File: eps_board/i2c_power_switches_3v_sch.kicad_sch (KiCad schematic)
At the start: 10 parts, among them U30 MCP23017T-E/SS

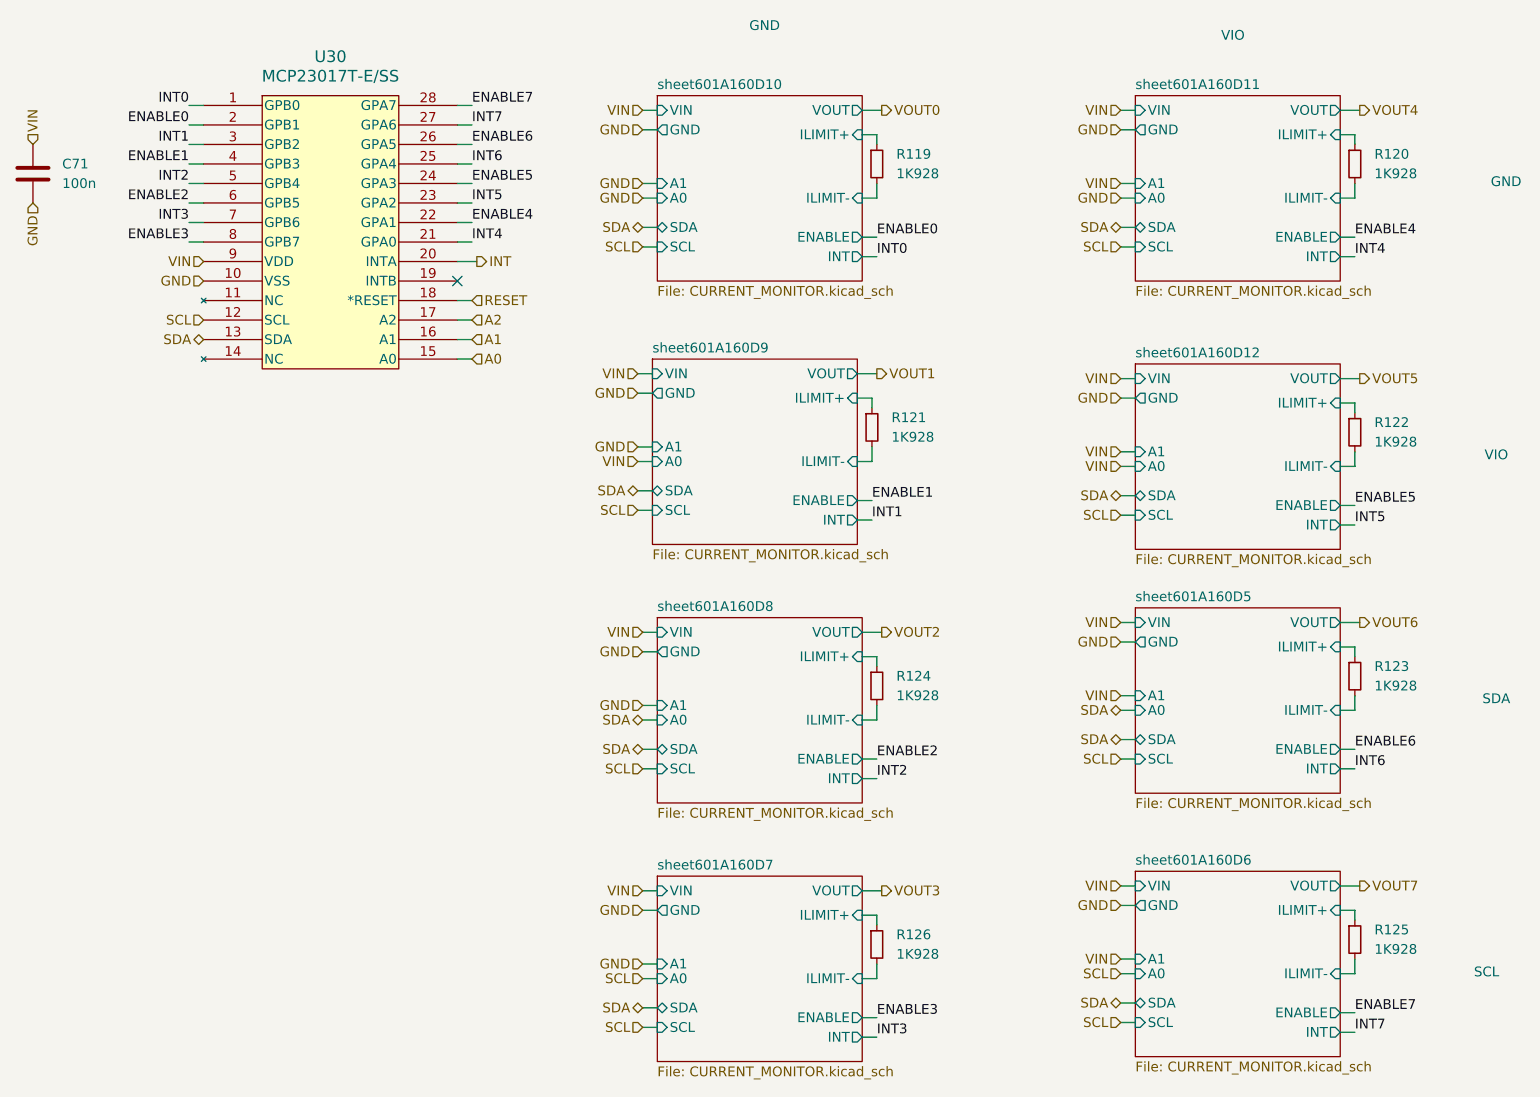
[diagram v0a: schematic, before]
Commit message: simply eps and automate startup conditions
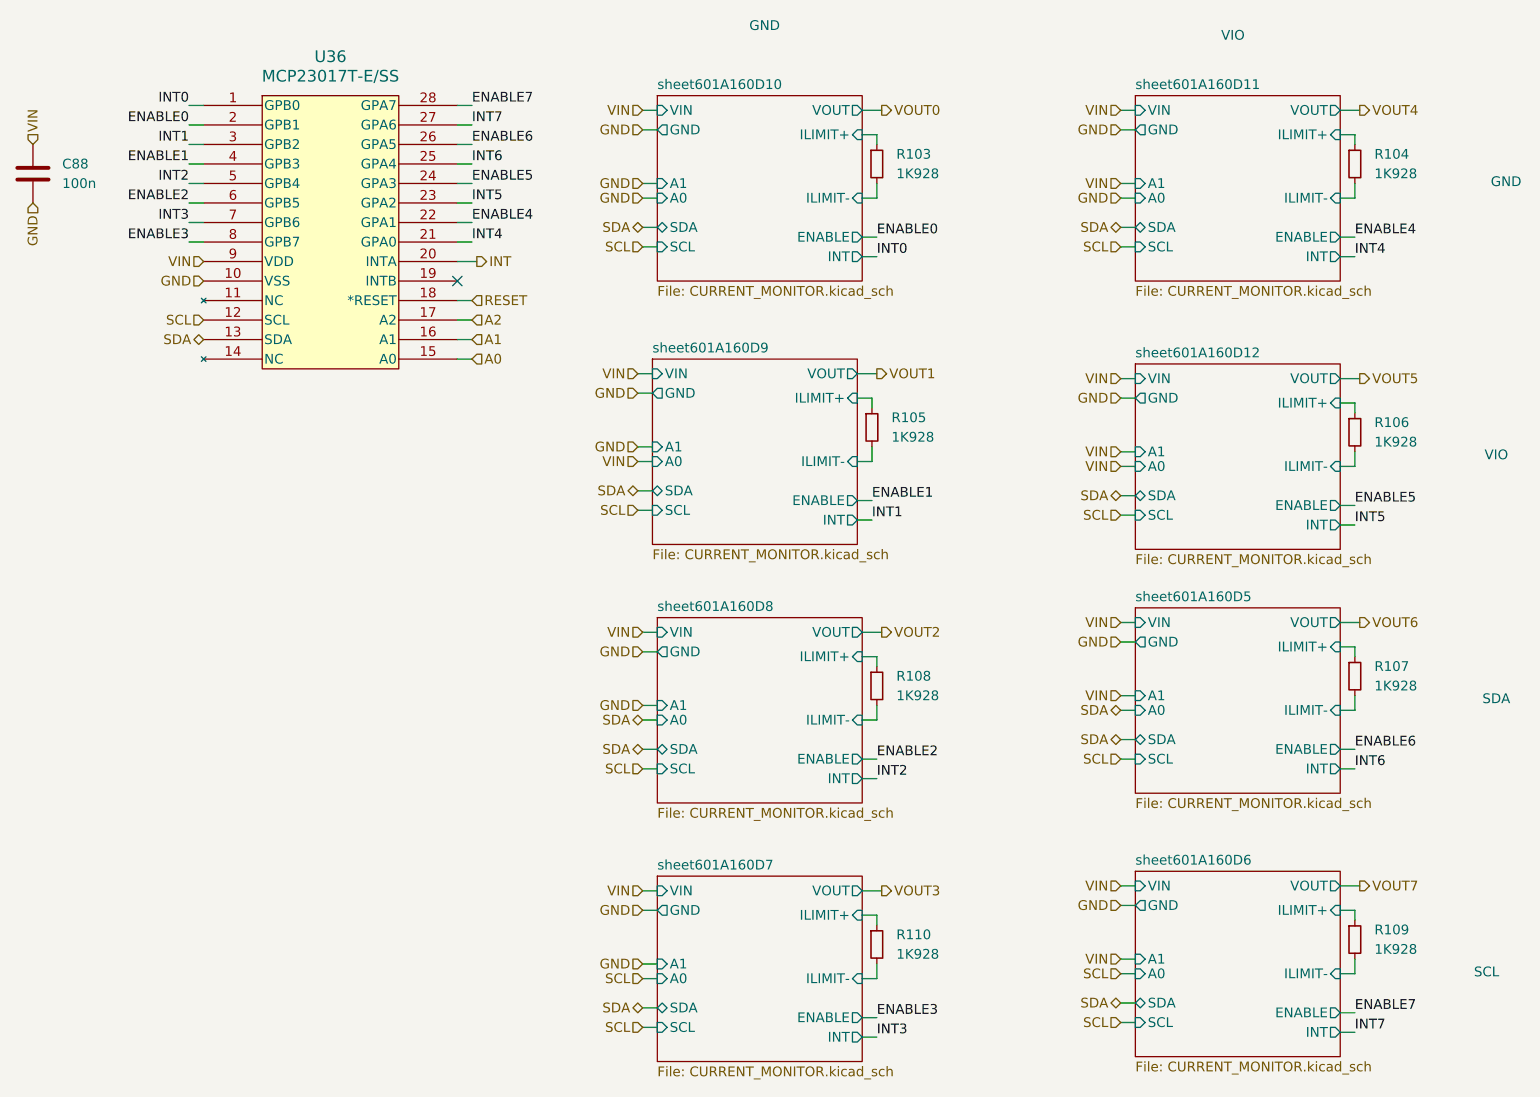
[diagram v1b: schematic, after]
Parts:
- renumbered C71 to C88, R119 to R103, R120 to R104, R121 to R105, R122 to R106, R123 to R107, R124 to R108, R125 to R109, R126 to R110, U30 to U36
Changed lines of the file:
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@@
 		(dnp no)
 		(fields_autoplaced yes)
-		(property "Reference" "U30"
+		(property "Reference" "U36"
 			(at 60.325 27.94 0)
 			(effects
@@
 			(project ""
 				(path "/05170af6-30ef-4c3a-b972-f098085da1bc/365e30aa-57e3-49e2-b136-6964bfe03313"
-					(reference "U30")
-					(unit 1)
-				)
-				(path "/05170af6-30ef-4c3a-b972-f098085da1bc/87d4360e-0b9f-4926-a66e-357599f9c0d1"
-					(reference "U48")
+					(reference "U36")
+					(unit 1)
+				)
+				(path "/05170af6-30ef-4c3a-b972-f098085da1bc/87d4360e-0b9f-4926-a66e-357599f9c0d1"
+					(reference "U56")
 					(unit 1)
 				)
@@
 		(dnp no)
 		(fields_autoplaced yes)
-		(property "Reference" "R123"
+		(property "Reference" "R107"
 			(at 196.215 107.3149 0)
 			(effects
@@
 			(project "EPS"
 				(path "/05170af6-30ef-4c3a-b972-f098085da1bc/365e30aa-57e3-49e2-b136-6964bfe03313"
-					(reference "R123")
-					(unit 1)
-				)
-				(path "/05170af6-30ef-4c3a-b972-f098085da1bc/87d4360e-0b9f-4926-a66e-357599f9c0d1"
-					(reference "R149")
+					(reference "R107")
+					(unit 1)
+				)
+				(path "/05170af6-30ef-4c3a-b972-f098085da1bc/87d4360e-0b9f-4926-a66e-357599f9c0d1"
+					(reference "R147")
 					(unit 1)
 				)
@@
 		(dnp no)
 		(fields_autoplaced yes)
-		(property "Reference" "R122"
+		(property "Reference" "R106"
 			(at 196.215 75.5649 0)
 			(effects
@@
 			(project "EPS"
 				(path "/05170af6-30ef-4c3a-b972-f098085da1bc/365e30aa-57e3-49e2-b136-6964bfe03313"
-					(reference "R122")
-					(unit 1)
-				)
-				(path "/05170af6-30ef-4c3a-b972-f098085da1bc/87d4360e-0b9f-4926-a66e-357599f9c0d1"
-					(reference "R148")
+					(reference "R106")
+					(unit 1)
+				)
+				(path "/05170af6-30ef-4c3a-b972-f098085da1bc/87d4360e-0b9f-4926-a66e-357599f9c0d1"
+					(reference "R146")
 					(unit 1)
 				)
@@
 		(dnp no)
 		(fields_autoplaced yes)
-		(property "Reference" "R124"
+		(property "Reference" "R108"
 			(at 133.985 108.5849 0)
 			(effects
@@
 			(project "EPS"
 				(path "/05170af6-30ef-4c3a-b972-f098085da1bc/365e30aa-57e3-49e2-b136-6964bfe03313"
-					(reference "R124")
-					(unit 1)
-				)
-				(path "/05170af6-30ef-4c3a-b972-f098085da1bc/87d4360e-0b9f-4926-a66e-357599f9c0d1"
-					(reference "R150")
+					(reference "R108")
+					(unit 1)
+				)
+				(path "/05170af6-30ef-4c3a-b972-f098085da1bc/87d4360e-0b9f-4926-a66e-357599f9c0d1"
+					(reference "R148")
 					(unit 1)
 				)
@@
 		(dnp no)
 		(fields_autoplaced yes)
-		(property "Reference" "R125"
+		(property "Reference" "R109"
 			(at 196.215 141.6049 0)
 			(effects
@@
 			(project "EPS"
 				(path "/05170af6-30ef-4c3a-b972-f098085da1bc/365e30aa-57e3-49e2-b136-6964bfe03313"
-					(reference "R125")
-					(unit 1)
-				)
-				(path "/05170af6-30ef-4c3a-b972-f098085da1bc/87d4360e-0b9f-4926-a66e-357599f9c0d1"
-					(reference "R151")
+					(reference "R109")
+					(unit 1)
+				)
+				(path "/05170af6-30ef-4c3a-b972-f098085da1bc/87d4360e-0b9f-4926-a66e-357599f9c0d1"
+					(reference "R149")
 					(unit 1)
 				)
@@
 		(dnp no)
 		(fields_autoplaced yes)
-		(property "Reference" "R119"
+		(property "Reference" "R103"
 			(at 133.985 40.6399 0)
 			(effects
@@
 			(project "EPS"
 				(path "/05170af6-30ef-4c3a-b972-f098085da1bc/365e30aa-57e3-49e2-b136-6964bfe03313"
-					(reference "R119")
-					(unit 1)
-				)
-				(path "/05170af6-30ef-4c3a-b972-f098085da1bc/87d4360e-0b9f-4926-a66e-357599f9c0d1"
-					(reference "R145")
+					(reference "R103")
+					(unit 1)
+				)
+				(path "/05170af6-30ef-4c3a-b972-f098085da1bc/87d4360e-0b9f-4926-a66e-357599f9c0d1"
+					(reference "R143")
 					(unit 1)
 				)
@@
 		(dnp no)
 		(fields_autoplaced yes)
-		(property "Reference" "R126"
+		(property "Reference" "R110"
 			(at 133.985 142.2399 0)
 			(effects
@@
 			(project "EPS"
 				(path "/05170af6-30ef-4c3a-b972-f098085da1bc/365e30aa-57e3-49e2-b136-6964bfe03313"
-					(reference "R126")
-					(unit 1)
-				)
-				(path "/05170af6-30ef-4c3a-b972-f098085da1bc/87d4360e-0b9f-4926-a66e-357599f9c0d1"
-					(reference "R152")
+					(reference "R110")
+					(unit 1)
+				)
+				(path "/05170af6-30ef-4c3a-b972-f098085da1bc/87d4360e-0b9f-4926-a66e-357599f9c0d1"
+					(reference "R150")
 					(unit 1)
 				)
@@
 		(dnp no)
 		(fields_autoplaced yes)
-		(property "Reference" "R121"
+		(property "Reference" "R105"
 			(at 133.35 74.9299 0)
 			(effects
@@
 			(project "EPS"
 				(path "/05170af6-30ef-4c3a-b972-f098085da1bc/365e30aa-57e3-49e2-b136-6964bfe03313"
-					(reference "R121")
-					(unit 1)
-				)
-				(path "/05170af6-30ef-4c3a-b972-f098085da1bc/87d4360e-0b9f-4926-a66e-357599f9c0d1"
-					(reference "R147")
+					(reference "R105")
+					(unit 1)
+				)
+				(path "/05170af6-30ef-4c3a-b972-f098085da1bc/87d4360e-0b9f-4926-a66e-357599f9c0d1"
+					(reference "R145")
 					(unit 1)
 				)
@@
 		(dnp no)
 		(fields_autoplaced yes)
-		(property "Reference" "C71"
+		(property "Reference" "C88"
 			(at 25.4 41.9099 0)
 			(effects
@@
 			(project "EPS"
 				(path "/05170af6-30ef-4c3a-b972-f098085da1bc/365e30aa-57e3-49e2-b136-6964bfe03313"
-					(reference "C71")
-					(unit 1)
-				)
-				(path "/05170af6-30ef-4c3a-b972-f098085da1bc/87d4360e-0b9f-4926-a66e-357599f9c0d1"
-					(reference "C97")
+					(reference "C88")
+					(unit 1)
+				)
+				(path "/05170af6-30ef-4c3a-b972-f098085da1bc/87d4360e-0b9f-4926-a66e-357599f9c0d1"
+					(reference "C116")
 					(unit 1)
 				)
@@
 		(dnp no)
 		(fields_autoplaced yes)
-		(property "Reference" "R120"
+		(property "Reference" "R104"
 			(at 196.215 40.6399 0)
 			(effects
@@
 			(project "EPS"
 				(path "/05170af6-30ef-4c3a-b972-f098085da1bc/365e30aa-57e3-49e2-b136-6964bfe03313"
-					(reference "R120")
-					(unit 1)
-				)
-				(path "/05170af6-30ef-4c3a-b972-f098085da1bc/87d4360e-0b9f-4926-a66e-357599f9c0d1"
-					(reference "R146")
-					(unit 1)
-				)
+					(reference "R104")
+					(unit 1)
+				)
+				(path "/05170af6-30ef-4c3a-b972-f098085da1bc/87d4360e-0b9f-4926-a66e-357599f9c0d1"
+					(reference "R144")
+					(unit 1)
+				)

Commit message: pcb and silk screen cleanup, interim
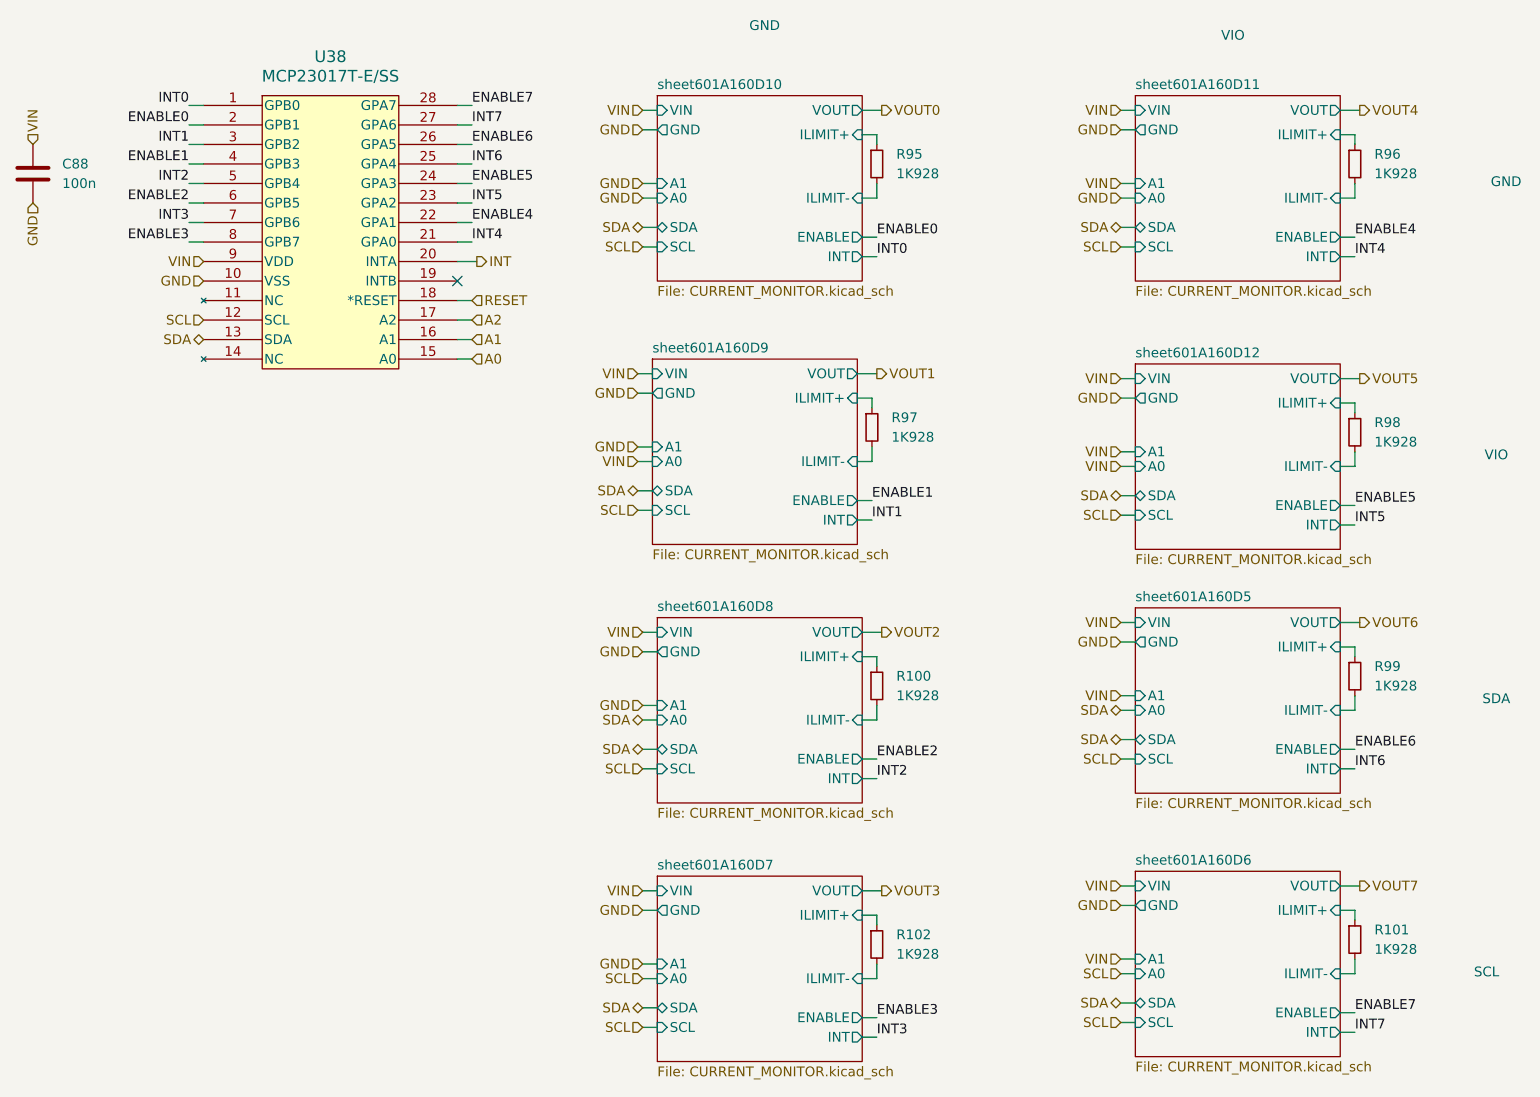
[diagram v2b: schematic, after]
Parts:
- renumbered R108 to R100, R109 to R101, R110 to R102, R103 to R95, R104 to R96, R105 to R97, R106 to R98, R107 to R99, U36 to U38
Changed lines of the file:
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@@
 		(dnp no)
 		(fields_autoplaced yes)
-		(property "Reference" "U36"
+		(property "Reference" "U38"
 			(at 60.325 27.94 0)
 			(effects
@@
 			(project ""
 				(path "/05170af6-30ef-4c3a-b972-f098085da1bc/365e30aa-57e3-49e2-b136-6964bfe03313"
-					(reference "U36")
-					(unit 1)
-				)
-				(path "/05170af6-30ef-4c3a-b972-f098085da1bc/87d4360e-0b9f-4926-a66e-357599f9c0d1"
-					(reference "U56")
+					(reference "U38")
+					(unit 1)
+				)
+				(path "/05170af6-30ef-4c3a-b972-f098085da1bc/87d4360e-0b9f-4926-a66e-357599f9c0d1"
+					(reference "U58")
 					(unit 1)
 				)
@@
 		(dnp no)
 		(fields_autoplaced yes)
-		(property "Reference" "R107"
+		(property "Reference" "R99"
 			(at 196.215 107.3149 0)
 			(effects
@@
 			(project "EPS"
 				(path "/05170af6-30ef-4c3a-b972-f098085da1bc/365e30aa-57e3-49e2-b136-6964bfe03313"
-					(reference "R107")
-					(unit 1)
-				)
-				(path "/05170af6-30ef-4c3a-b972-f098085da1bc/87d4360e-0b9f-4926-a66e-357599f9c0d1"
-					(reference "R147")
+					(reference "R99")
+					(unit 1)
+				)
+				(path "/05170af6-30ef-4c3a-b972-f098085da1bc/87d4360e-0b9f-4926-a66e-357599f9c0d1"
+					(reference "R139")
 					(unit 1)
 				)
@@
 		(dnp no)
 		(fields_autoplaced yes)
-		(property "Reference" "R106"
+		(property "Reference" "R98"
 			(at 196.215 75.5649 0)
 			(effects
@@
 			(project "EPS"
 				(path "/05170af6-30ef-4c3a-b972-f098085da1bc/365e30aa-57e3-49e2-b136-6964bfe03313"
-					(reference "R106")
-					(unit 1)
-				)
-				(path "/05170af6-30ef-4c3a-b972-f098085da1bc/87d4360e-0b9f-4926-a66e-357599f9c0d1"
-					(reference "R146")
+					(reference "R98")
+					(unit 1)
+				)
+				(path "/05170af6-30ef-4c3a-b972-f098085da1bc/87d4360e-0b9f-4926-a66e-357599f9c0d1"
+					(reference "R138")
 					(unit 1)
 				)
@@
 		(dnp no)
 		(fields_autoplaced yes)
-		(property "Reference" "R108"
+		(property "Reference" "R100"
 			(at 133.985 108.5849 0)
 			(effects
@@
 			(project "EPS"
 				(path "/05170af6-30ef-4c3a-b972-f098085da1bc/365e30aa-57e3-49e2-b136-6964bfe03313"
-					(reference "R108")
-					(unit 1)
-				)
-				(path "/05170af6-30ef-4c3a-b972-f098085da1bc/87d4360e-0b9f-4926-a66e-357599f9c0d1"
-					(reference "R148")
+					(reference "R100")
+					(unit 1)
+				)
+				(path "/05170af6-30ef-4c3a-b972-f098085da1bc/87d4360e-0b9f-4926-a66e-357599f9c0d1"
+					(reference "R140")
 					(unit 1)
 				)
@@
 		(dnp no)
 		(fields_autoplaced yes)
-		(property "Reference" "R109"
+		(property "Reference" "R101"
 			(at 196.215 141.6049 0)
 			(effects
@@
 			(project "EPS"
 				(path "/05170af6-30ef-4c3a-b972-f098085da1bc/365e30aa-57e3-49e2-b136-6964bfe03313"
-					(reference "R109")
-					(unit 1)
-				)
-				(path "/05170af6-30ef-4c3a-b972-f098085da1bc/87d4360e-0b9f-4926-a66e-357599f9c0d1"
-					(reference "R149")
+					(reference "R101")
+					(unit 1)
+				)
+				(path "/05170af6-30ef-4c3a-b972-f098085da1bc/87d4360e-0b9f-4926-a66e-357599f9c0d1"
+					(reference "R141")
 					(unit 1)
 				)
@@
 		(dnp no)
 		(fields_autoplaced yes)
-		(property "Reference" "R103"
+		(property "Reference" "R95"
 			(at 133.985 40.6399 0)
 			(effects
@@
 			(project "EPS"
 				(path "/05170af6-30ef-4c3a-b972-f098085da1bc/365e30aa-57e3-49e2-b136-6964bfe03313"
-					(reference "R103")
-					(unit 1)
-				)
-				(path "/05170af6-30ef-4c3a-b972-f098085da1bc/87d4360e-0b9f-4926-a66e-357599f9c0d1"
-					(reference "R143")
+					(reference "R95")
+					(unit 1)
+				)
+				(path "/05170af6-30ef-4c3a-b972-f098085da1bc/87d4360e-0b9f-4926-a66e-357599f9c0d1"
+					(reference "R135")
 					(unit 1)
 				)
@@
 		(dnp no)
 		(fields_autoplaced yes)
-		(property "Reference" "R110"
+		(property "Reference" "R102"
 			(at 133.985 142.2399 0)
 			(effects
@@
 			(project "EPS"
 				(path "/05170af6-30ef-4c3a-b972-f098085da1bc/365e30aa-57e3-49e2-b136-6964bfe03313"
-					(reference "R110")
-					(unit 1)
-				)
-				(path "/05170af6-30ef-4c3a-b972-f098085da1bc/87d4360e-0b9f-4926-a66e-357599f9c0d1"
-					(reference "R150")
+					(reference "R102")
+					(unit 1)
+				)
+				(path "/05170af6-30ef-4c3a-b972-f098085da1bc/87d4360e-0b9f-4926-a66e-357599f9c0d1"
+					(reference "R142")
 					(unit 1)
 				)
@@
 		(dnp no)
 		(fields_autoplaced yes)
-		(property "Reference" "R105"
+		(property "Reference" "R97"
 			(at 133.35 74.9299 0)
 			(effects
@@
 			(project "EPS"
 				(path "/05170af6-30ef-4c3a-b972-f098085da1bc/365e30aa-57e3-49e2-b136-6964bfe03313"
-					(reference "R105")
-					(unit 1)
-				)
-				(path "/05170af6-30ef-4c3a-b972-f098085da1bc/87d4360e-0b9f-4926-a66e-357599f9c0d1"
-					(reference "R145")
+					(reference "R97")
+					(unit 1)
+				)
+				(path "/05170af6-30ef-4c3a-b972-f098085da1bc/87d4360e-0b9f-4926-a66e-357599f9c0d1"
+					(reference "R137")
 					(unit 1)
 				)
@@
 		(dnp no)
 		(fields_autoplaced yes)
-		(property "Reference" "R104"
+		(property "Reference" "R96"
 			(at 196.215 40.6399 0)
 			(effects
@@
 			(project "EPS"
 				(path "/05170af6-30ef-4c3a-b972-f098085da1bc/365e30aa-57e3-49e2-b136-6964bfe03313"
-					(reference "R104")
-					(unit 1)
-				)
-				(path "/05170af6-30ef-4c3a-b972-f098085da1bc/87d4360e-0b9f-4926-a66e-357599f9c0d1"
-					(reference "R144")
-					(unit 1)
-				)
+					(reference "R96")
+					(unit 1)
+				)
+				(path "/05170af6-30ef-4c3a-b972-f098085da1bc/87d4360e-0b9f-4926-a66e-357599f9c0d1"
+					(reference "R136")
+					(unit 1)
+				)
